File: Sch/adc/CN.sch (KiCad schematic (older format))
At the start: 19 parts, among them J2 Header5, P1 CONN_02X40, U1 LTC2292

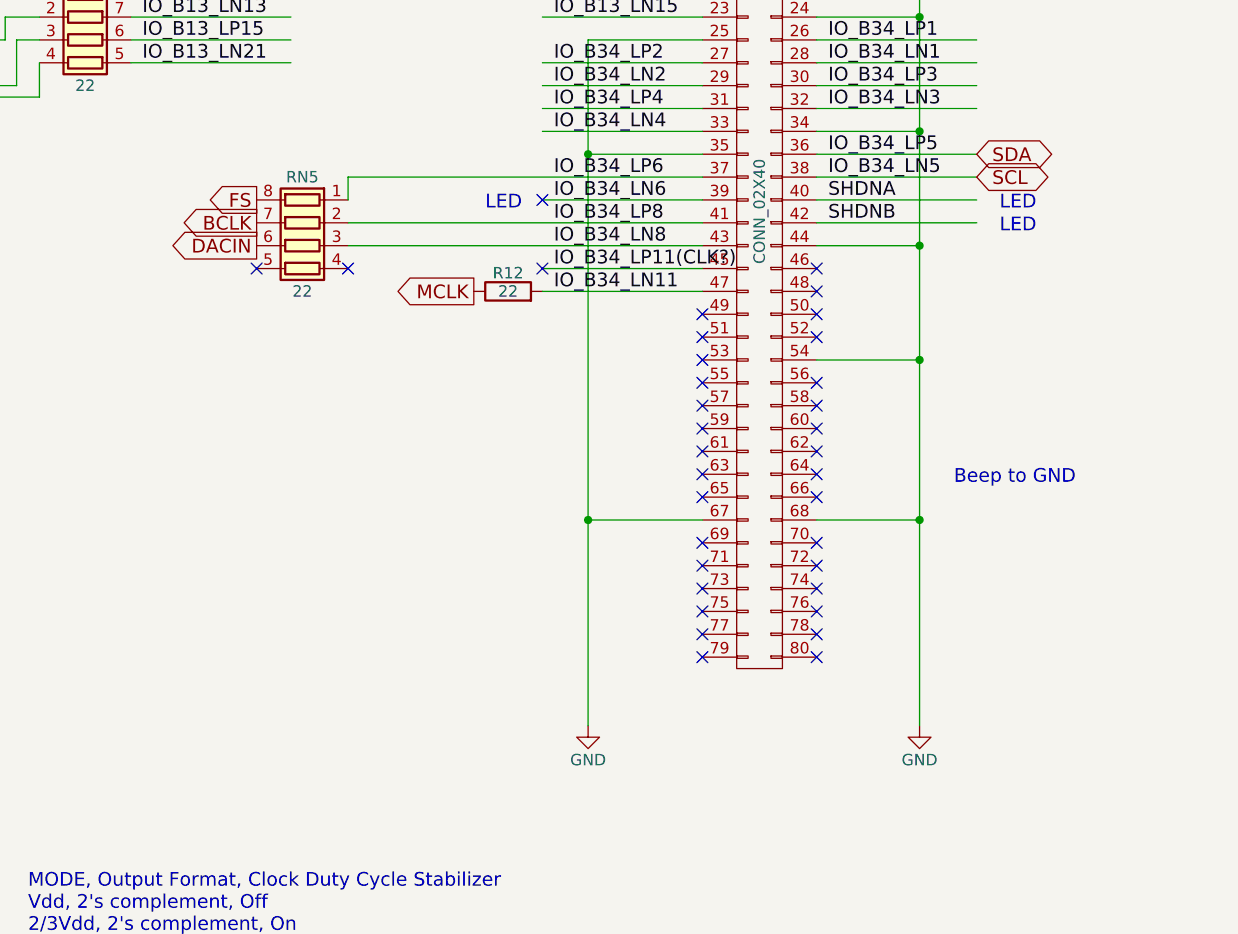
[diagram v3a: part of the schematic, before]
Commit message: Add pull-down to BP net. Remove RF amp of 2nd input to the ADC.
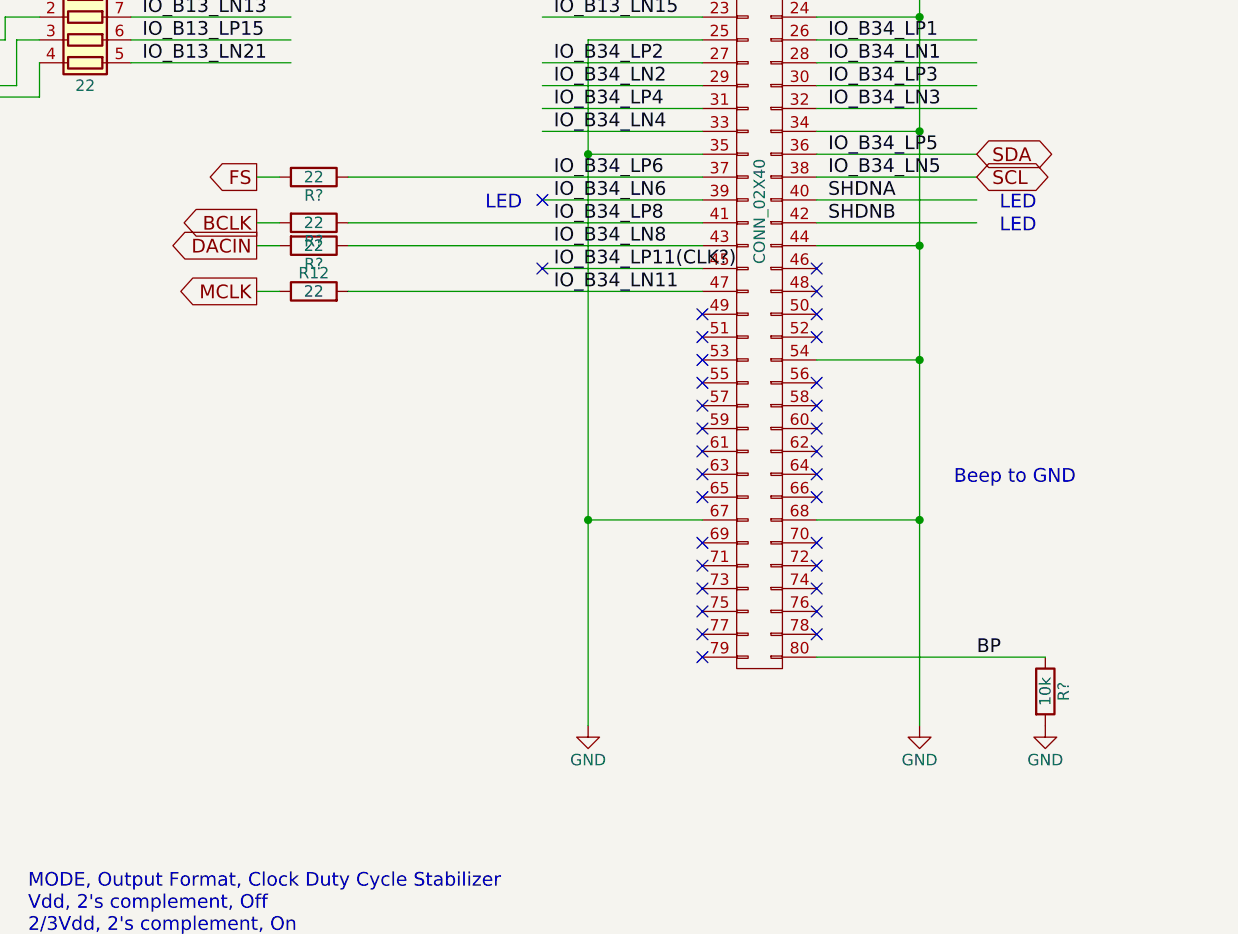
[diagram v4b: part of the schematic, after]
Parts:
- removed RN5: 22, adc_lib:EXB-38V220JV, symbol R_Pack04
- added R? (x3): 22, symbol R
- added R?: 10k, adc_lib:R0603, symbol R
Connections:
- net labels added: BP
- wire segments 135 -> 139
- no-connect marks 60 -> 57
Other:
- moved on the sheet: R12
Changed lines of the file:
@@
 	6650 3950 5950 3950
 Wire Wire Line
-	6650 4050 5950 4050
+	5100 4050 6650 4050
 Wire Wire Line
 	7150 2450 7850 2450
@@
 Text Notes 750  3300 0    60   ~ 0
 High=nap mode
-Text GLabel 4700 3650 0    60   Output ~ 0
+Text GLabel 4700 3550 0    60   Output ~ 0
 FS
 Text GLabel 4700 3750 0    60   Output ~ 0
@@
 Text GLabel 4700 3850 0    60   Output ~ 0
 DACIN
-Text GLabel 5650 4050 0    60   Output ~ 0
+Text GLabel 4700 4050 0    60   Output ~ 0
 MCLK
 Text GLabel 7850 3550 2    60   BiDi ~ 0
@@
 SDA
 $Comp
-L R_Pack04 RN5
-U 1 1 58A9A1DD
-P 4900 3850
-F 0 "RN5" V 4600 3850 50  0000 C CNN
-F 1 "22" V 5100 3850 50  0000 C CNN
-F 2 "adc_lib:EXB-38V220JV" V 5175 3850 50  0001 C CNN
-F 3 "" H 4900 3850 50  0000 C CNN
-	1    4900 3850
-	0    -1   1    0
-$EndComp
-$Comp
 L R R12
 U 1 1 58A9A823
-P 5800 4050
-F 0 "R12" V 5880 4050 50  0000 C CNN
-F 1 "22" V 5800 4050 50  0000 C CNN
-F 2 "adc_lib:R0603" V 5730 4050 50  0001 C CNN
-F 3 "" H 5800 4050 50  0000 C CNN
-	1    5800 4050
+P 4950 4050
+F 0 "R12" V 5030 4050 50  0000 C CNN
+F 1 "22" V 4950 4050 50  0000 C CNN
+F 2 "adc_lib:R0603" V 4880 4050 50  0001 C CNN
+F 3 "" H 4950 4050 50  0000 C CNN
+	1    4950 4050
 	0    -1   -1   0
 $EndComp
@@
 Wire Wire Line
 	7150 2550 8350 2550
-Wire Wire Line
-	5100 3550 5100 3650
-NoConn ~ 4700 3950
-NoConn ~ 5100 3950
 NoConn ~ 5950 2250
 NoConn ~ 5950 2150
@@
 NoConn ~ 8350 2550
 NoConn ~ 5950 2550
-NoConn ~ 7150 5650
 Text Notes 7750 4900 0    60   ~ 0
 Beep to GND
@@
 	2950 6050 3150 6050
 Connection ~ 3150 6050
+$Comp
+L R R?
+U 1 1 59574E56
+P 4950 3750
+F 0 "R?" V 5030 3750 50  0000 C CNN
+F 1 "22" V 4950 3750 50  0000 C CNN
+F 2 "" V 4880 3750 50  0000 C CNN
+F 3 "" H 4950 3750 50  0000 C CNN
+	1    4950 3750
+	0    1    1    0
+$EndComp
+$Comp
+L R R?
+U 1 1 59574F08
+P 4950 3550
+F 0 "R?" V 5030 3550 50  0000 C CNN
+F 1 "22" V 4950 3550 50  0000 C CNN
+F 2 "" V 4880 3550 50  0000 C CNN
+F 3 "" H 4950 3550 50  0000 C CNN
+	1    4950 3550
+	0    1    1    0
+$EndComp
+$Comp
+L R R?
+U 1 1 59574F5D
+P 4950 3850
+F 0 "R?" V 5030 3850 50  0000 C CNN
+F 1 "22" V 4950 3850 50  0000 C CNN
+F 2 "" V 4880 3850 50  0000 C CNN
+F 3 "" H 4950 3850 50  0000 C CNN
+	1    4950 3850
+	0    1    1    0
+$EndComp
+Wire Wire Line
+	4700 3550 4800 3550
+Wire Wire Line
+	4700 3750 4800 3750
+Wire Wire Line
+	4700 3850 4800 3850
+Wire Wire Line
+	4700 4050 4800 4050
+Wire Wire Line
+	7150 5650 8150 5650
+Text Label 7850 5650 0    60   ~ 0
+BP
+$Comp
+L R R?
+U 1 1 5957B758
+P 8150 5800
+F 0 "R?" V 8230 5800 50  0000 C CNN
+F 1 "10k" V 8150 5800 50  0000 C CNN
+F 2 "adc_lib:R0603" V 8080 5800 50  0001 C CNN
+F 3 "" H 8150 5800 50  0000 C CNN
+	1    8150 5800
+	1    0    0    -1
+$EndComp
+$Comp
+L GND #PWR?
+U 1 1 5957B7EE
+P 8150 5950
+F 0 "#PWR?" H 8150 5700 50  0001 C CNN
+F 1 "GND" H 8150 5800 50  0000 C CNN
+F 2 "" H 8150 5950 50  0000 C CNN
+F 3 "" H 8150 5950 50  0000 C CNN
+	1    8150 5950
+	1    0    0    -1
+$EndComp
 $EndSCHEMATC

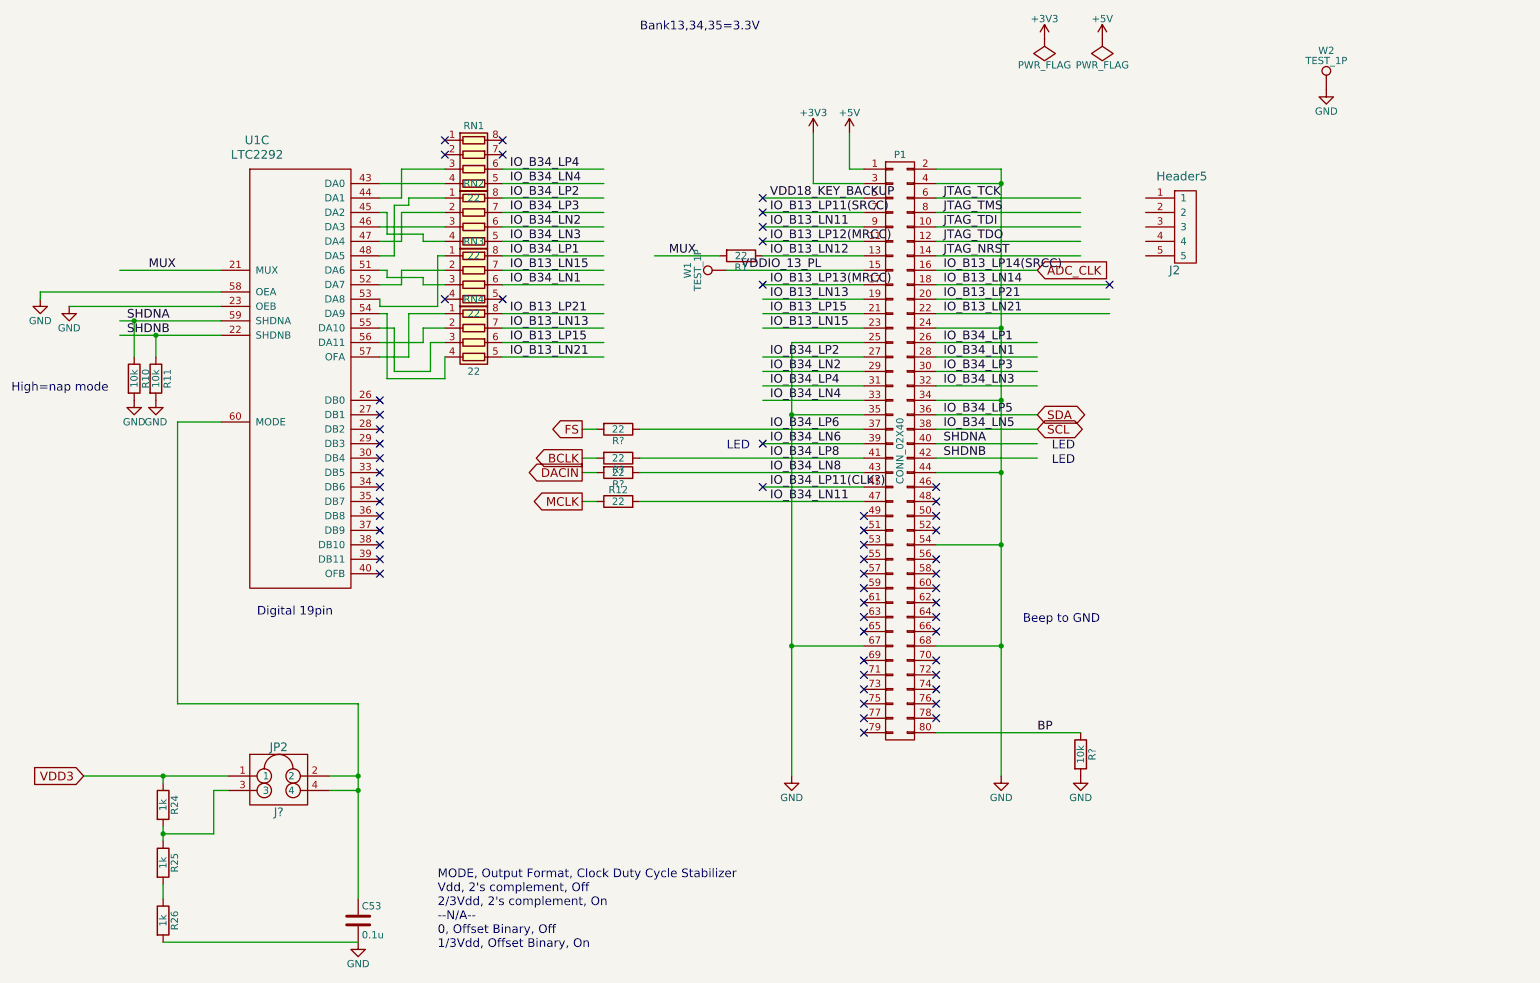
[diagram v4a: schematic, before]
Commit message: Analog front end is removed from the ADC board. ADC board is done
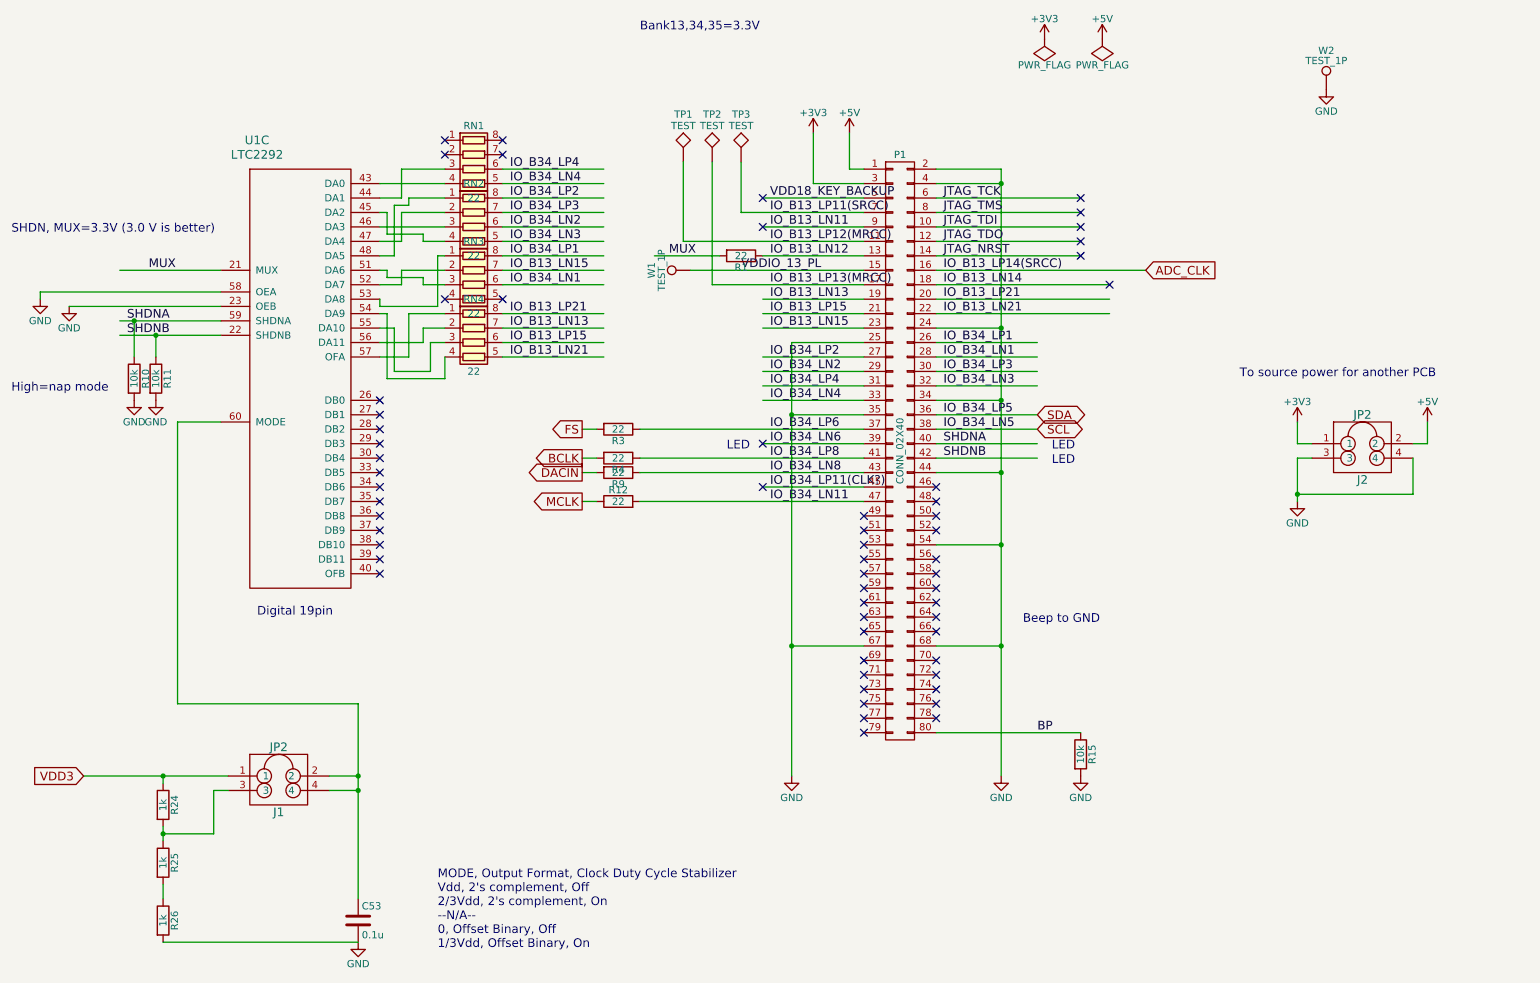
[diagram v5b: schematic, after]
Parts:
- removed J2: Header5, adc_lib:M20-9990546, symbol Header5
- added J2: JP2, symbol JP2
- added TP1, TP2, TP3: TEST, symbol TEST
- gave numbers to parts that had none: 5
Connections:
- wire segments 139 -> 150
- no-connect marks 57 -> 59
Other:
- note added: "SHDN, MUX=3.3V (3.0 V is better)"
- note added: "To source power for another PCB"
- moved on the sheet: W1
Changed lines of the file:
@@
 Text Label 7200 2350 0    60   ~ 0
 JTAG_NRST
-$Comp
-L Header5 J2
-U 1 1 58A52616
-P 8800 2150
-F 0 "J2" H 8800 1850 60  0000 C CNN
-F 1 "Header5" H 8850 2500 60  0000 C CNN
-F 2 "adc_lib:M20-9990546" H 8800 2250 60  0001 C CNN
-F 3 "" H 8800 2250 60  0001 C CNN
-	1    8800 2150
-	1    0    0    -1
-$EndComp
 NoConn ~ 5950 1950
-Text GLabel 7850 2450 2    60   Input ~ 0
+Text GLabel 8600 2450 2    60   Input ~ 0
 ADC_CLK
 $Comp
@@
 	6300 1850 6650 1850
 Wire Wire Line
-	6650 2050 5950 2050
+	5800 2050 6650 2050
 Wire Wire Line
 	6650 2150 5950 2150
 Wire Wire Line
-	6650 2250 5950 2250
+	5400 2250 6650 2250
 Wire Wire Line
 	6650 2350 5950 2350
 Wire Wire Line
-	6650 2550 5950 2550
+	5600 2550 6650 2550
 Wire Wire Line
 	6650 2650 5950 2650
@@
 	5100 4050 6650 4050
 Wire Wire Line
-	7150 2450 7850 2450
+	7150 2450 8600 2450
 Wire Wire Line
 	7150 2650 8350 2650
@@
 	1900 5450 3150 5450
 Wire Wire Line
-	6650 2450 5700 2450
+	6650 2450 5450 2450
 Wire Wire Line
 	6650 1950 5950 1950
@@
 L TEST_1P W1
 U 1 1 58A9D9D4
-P 5700 2450
-F 0 "W1" H 5700 2720 50  0000 C CNN
-F 1 "TEST_1P" H 5700 2650 50  0000 C CNN
-F 2 "adc_lib:68000-401HLF" H 5900 2450 50  0001 C CNN
-F 3 "" H 5900 2450 50  0000 C CNN
-	1    5700 2450
+P 5450 2450
+F 0 "W1" H 5450 2720 50  0000 C CNN
+F 1 "TEST_1P" H 5450 2650 50  0000 C CNN
+F 2 "adc_lib:68000-401HLF" H 5650 2450 50  0001 C CNN
+F 3 "" H 5650 2450 50  0000 C CNN
+	1    5450 2450
 	0    -1   -1   0
 $EndComp
@@
 Wire Wire Line
 	7150 2550 8350 2550
-NoConn ~ 5950 2250
 NoConn ~ 5950 2150
 $Comp
@@
 Text Label 1700 2450 0    60   ~ 0
 MUX
-NoConn ~ 5950 2050
 NoConn ~ 8350 2550
-NoConn ~ 5950 2550
 Text Notes 7750 4900 0    60   ~ 0
 Beep to GND
 $Comp
-L JP2 J?
+L JP2 J1
 U 1 1 594BFF08
 P 2600 5950
-F 0 "J?" H 2600 5700 60  0000 C CNN
+F 0 "J1" H 2600 5700 60  0000 C CNN
 F 1 "JP2" H 2600 6150 60  0000 C CNN
 F 2 "" H 2550 6050 60  0001 C CNN
@@
 Connection ~ 3150 6050
 $Comp
-L R R?
+L R R4
 U 1 1 59574E56
 P 4950 3750
-F 0 "R?" V 5030 3750 50  0000 C CNN
+F 0 "R4" V 5030 3750 50  0000 C CNN
 F 1 "22" V 4950 3750 50  0000 C CNN
 F 2 "" V 4880 3750 50  0000 C CNN
@@
 $EndComp
 $Comp
-L R R?
+L R R3
 U 1 1 59574F08
 P 4950 3550
-F 0 "R?" V 5030 3550 50  0000 C CNN
+F 0 "R3" V 5030 3550 50  0000 C CNN
 F 1 "22" V 4950 3550 50  0000 C CNN
 F 2 "" V 4880 3550 50  0000 C CNN
@@
 $EndComp
 $Comp
-L R R?
+L R R9
 U 1 1 59574F5D
 P 4950 3850
-F 0 "R?" V 5030 3850 50  0000 C CNN
+F 0 "R9" V 5030 3850 50  0000 C CNN
 F 1 "22" V 4950 3850 50  0000 C CNN
 F 2 "" V 4880 3850 50  0000 C CNN
@@
 BP
 $Comp
-L R R?
+L R R15
 U 1 1 5957B758
 P 8150 5800
-F 0 "R?" V 8230 5800 50  0000 C CNN
+F 0 "R15" V 8230 5800 50  0000 C CNN
 F 1 "10k" V 8150 5800 50  0000 C CNN
 F 2 "adc_lib:R0603" V 8080 5800 50  0001 C CNN
@@
 $EndComp
 $Comp
-L GND #PWR?
+L GND #PWR015
 U 1 1 5957B7EE
 P 8150 5950
-F 0 "#PWR?" H 8150 5700 50  0001 C CNN
+F 0 "#PWR015" H 8150 5700 50  0001 C CNN
 F 1 "GND" H 8150 5800 50  0000 C CNN
 F 2 "" H 8150 5950 50  0000 C CNN
@@
 	1    0    0    -1
 $EndComp
+$Comp
+L +3V3 #PWR016
+U 1 1 59761EBD
+P 9650 3500
+F 0 "#PWR016" H 9650 3350 50  0001 C CNN
+F 1 "+3V3" H 9650 3640 50  0000 C CNN
+F 2 "" H 9650 3500 50  0000 C CNN
+F 3 "" H 9650 3500 50  0000 C CNN
+	1    9650 3500
+	1    0    0    -1
+$EndComp
+$Comp
+L +5V #PWR017
+U 1 1 59761EC3
+P 10550 3500
+F 0 "#PWR017" H 10550 3350 50  0001 C CNN
+F 1 "+5V" H 10550 3640 50  0000 C CNN
+F 2 "" H 10550 3500 50  0000 C CNN
+F 3 "" H 10550 3500 50  0000 C CNN
+	1    10550 3500
+	1    0    0    -1
+$EndComp
+$Comp
+L GND #PWR018
+U 1 1 59762403
+P 9650 4050
+F 0 "#PWR018" H 9650 3800 50  0001 C CNN
+F 1 "GND" H 9650 3900 50  0000 C CNN
+F 2 "" H 9650 4050 50  0000 C CNN
+F 3 "" H 9650 4050 50  0000 C CNN
+	1    9650 4050
+	1    0    0    -1
+$EndComp
+$Comp
+L JP2 J2
+U 1 1 59776382
+P 10100 3650
+F 0 "J2" H 10100 3400 60  0000 C CNN
+F 1 "JP2" H 10100 3850 60  0000 C CNN
+F 2 "" H 10050 3750 60  0001 C CNN
+F 3 "" H 10050 3750 60  0001 C CNN
+	1    10100 3650
+	1    0    0    -1
+$EndComp
+Wire Wire Line
+	9750 3750 9650 3750
+Wire Wire Line
+	9650 3750 9650 4050
+Wire Wire Line
+	10450 3750 10450 4000
+Wire Wire Line
+	10450 4000 9650 4000
+Connection ~ 9650 4000
+Wire Wire Line
+	9650 3500 9650 3650
+Wire Wire Line
+	9650 3650 9750 3650
+Wire Wire Line
+	10450 3650 10550 3650
+Wire Wire Line
+	10550 3650 10550 3500
+Text Notes 750  2200 0    60   ~ 0
+SHDN, MUX=3.3V (3.0 V is better)
+Text Notes 9250 3200 0    60   ~ 0
+To source power for another PCB
+$Comp
+L TEST TP3
+U 1 1 5977AB09
+P 5800 1700
+F 0 "TP3" H 5800 2000 50  0000 C BNN
+F 1 "TEST" H 5800 1950 50  0000 C CNN
+F 2 "" H 5800 1700 50  0000 C CNN
+F 3 "" H 5800 1700 50  0000 C CNN
+	1    5800 1700
+	1    0    0    -1
+$EndComp
+$Comp
+L TEST TP2
+U 1 1 5977AB92
+P 5600 1700
+F 0 "TP2" H 5600 2000 50  0000 C BNN
+F 1 "TEST" H 5600 1950 50  0000 C CNN
+F 2 "" H 5600 1700 50  0000 C CNN
+F 3 "" H 5600 1700 50  0000 C CNN
+	1    5600 1700
+	1    0    0    -1
+$EndComp
+$Comp
+L TEST TP1
+U 1 1 5977ABD5
+P 5400 1700
+F 0 "TP1" H 5400 2000 50  0000 C BNN
+F 1 "TEST" H 5400 1950 50  0000 C CNN
+F 2 "" H 5400 1700 50  0000 C CNN
+F 3 "" H 5400 1700 50  0000 C CNN
+	1    5400 1700
+	1    0    0    -1
+$EndComp
+Wire Wire Line
+	5800 1700 5800 2050
+Wire Wire Line
+	5400 1700 5400 2250
+Wire Wire Line
+	5600 1700 5600 2550
+NoConn ~ 8150 1950
+NoConn ~ 8150 2050
+NoConn ~ 8150 2150
+NoConn ~ 8150 2250
+NoConn ~ 8150 2350
 $EndSCHEMATC
